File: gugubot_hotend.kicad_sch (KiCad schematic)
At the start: 79 parts, among them J1 Power +24V, J2 TEMP_SENSOR, J3 X_ENDSTOP, J4 PROBE, J5 FAN1, J6 FAN2, J7 Heater, J8 Extruder_motor, J9 USB_C_Receptacle_USB2.0, Q1 WST4041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

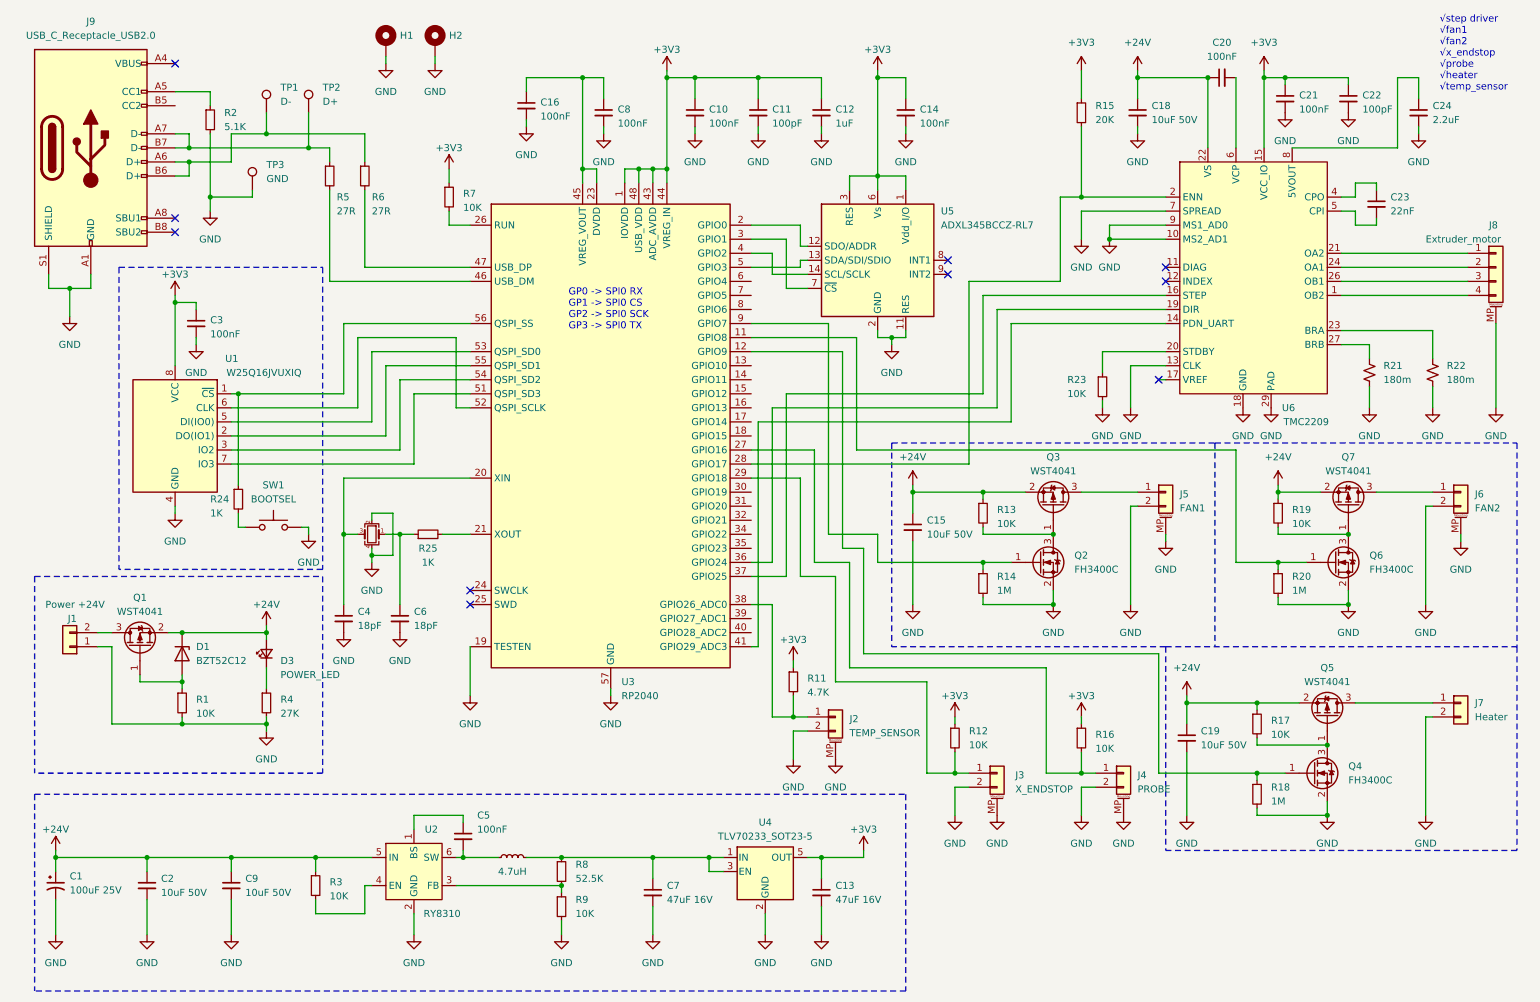
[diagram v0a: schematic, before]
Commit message: add hall board
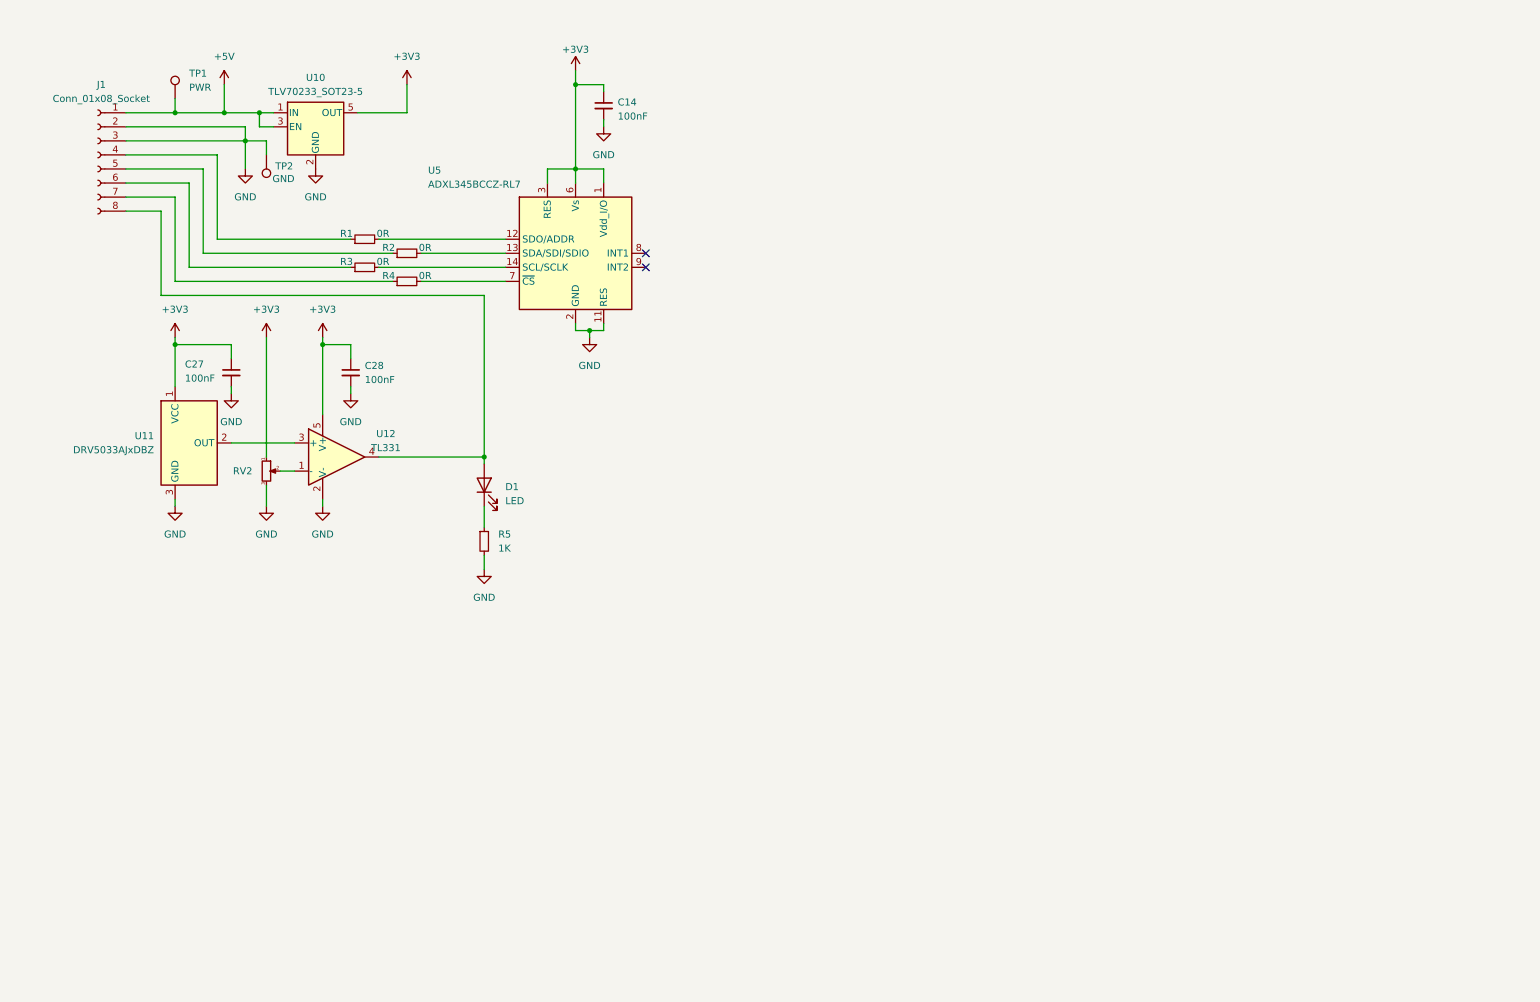
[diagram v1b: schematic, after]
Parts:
- removed C1: 100uF 25V, Capacitor_SMD:CP_Elec_6.3x5.8, symbol Device:C_Polarized_Small_US
- removed C10, C16, C20, C21, C3, C5, C8: 100nF, Capacitor_SMD:C_0402_1005Metric, symbol Device:C_Small
- removed C11, C22: 100pF, Capacitor_SMD:C_0402_1005Metric, symbol Device:C_Small
- removed C12: 1uF, Capacitor_SMD:C_0402_1005Metric, symbol Device:C_Small
- removed C13, C7: 47uF 16V, Capacitor_SMD:C_1210_3225Metric, symbol Device:C_Small
- removed C15, C18, C19, C2, C9: 10uF 50V, Capacitor_SMD:C_1210_3225Metric, symbol Device:C_Small
- removed C23: 22nF, Capacitor_SMD:C_0402_1005Metric, symbol Device:C_Small
- removed C24: 2.2uF, Capacitor_SMD:C_0402_1005Metric, symbol Device:C_Small
- removed C4, C6: 18pF, Capacitor_SMD:C_0402_1005Metric, symbol Device:C_Small
- removed D1: BZT52C12, Diode_SMD:D_SOD-123, symbol Diode:ZMMxx
- removed D3: POWER_LED, LED_SMD:LED_0603_1608Metric, symbol Device:LED_Small
- removed H1, H2: MountingHole_Pad, MountingHole:MountingHole_3.2mm_M3_Pad_Via, symbol Mechanical:MountingHole_Pad
- removed J1: Power +24V, TerminalBlock_TE-Connectivity:TerminalBlock_TE_282834-2_1x02_P2.54mm_Horizontal, symbol Connector_Generic:Conn_01x02
- removed J2: TEMP_SENSOR, Connector_GH:GH_1.25_1x02_Horizontal, symbol Connector_Generic_MountingPin:Conn_01x02_MountingPin
- removed J3: X_ENDSTOP, Connector_GH:GH_1.25_1x02_Horizontal, symbol Connector_Generic_MountingPin:Conn_01x02_MountingPin
- removed J4: PROBE, Connector_GH:GH_1.25_1x02_Horizontal, symbol Connector_Generic_MountingPin:Conn_01x02_MountingPin
- removed J5: FAN1, Connector_GH:GH_1.25_1x02_Horizontal, symbol Connector_Generic_MountingPin:Conn_01x02_MountingPin
- removed J6: FAN2, Connector_GH:GH_1.25_1x02_Horizontal, symbol Connector_Generic_MountingPin:Conn_01x02_MountingPin
- removed J7: Heater, TerminalBlock_TE-Connectivity:TerminalBlock_TE_282834-2_1x02_P2.54mm_Horizontal, symbol Connector_Generic:Conn_01x02
- removed J8: Extruder_motor, Connector_GH:GH_1.25_1x04_Veritical, symbol Connector_Generic_MountingPin:Conn_01x04_MountingPin
- removed J9: USB_C_Receptacle_USB2.0, Connector_USB:USB_C_Receptacle_G-Switch_GT-USB-7010ASV, symbol Connector:USB_C_Receptacle_USB2.0
- removed L1: 4.7uH, Inductor_SMD:L_1008_2520Metric, symbol Device:L_Small
- removed Q1, Q3, Q5, Q7: WST4041, Package_TO_SOT_SMD:SOT-23, symbol Device:Q_PMOS_GSD
- removed Q2, Q4, Q6: FH3400C, Package_TO_SOT_SMD:SOT-23, symbol Device:Q_NMOS_GSD
- removed R11: 4.7K, Resistor_SMD:R_0402_1005Metric, symbol Device:R_Small
- removed R12, R13, R16, R17, R19, R23, R7, R9: 10K, Resistor_SMD:R_0402_1005Metric, symbol Device:R_Small
- removed R14, R18, R20: 1M, Resistor_SMD:R_0402_1005Metric, symbol Device:R_Small
- removed R15: 20K, Resistor_SMD:R_0402_1005Metric, symbol Device:R_Small
- removed R21, R22: 180m, Resistor_SMD:R_1206_3216Metric, symbol Device:R_Small_US
- removed R24, R25: 1K, Resistor_SMD:R_0402_1005Metric, symbol Device:R_Small
- removed R6: 27R, Resistor_SMD:R_0402_1005Metric, symbol Device:R_Small
- removed R8: 52.5K, Resistor_SMD:R_0402_1005Metric, symbol Device:R_Small
- removed SW1: BOOTSEL, Button_Switch_SMD:SW_SPST_CK_RS282G05A3, symbol Switch:SW_Push
- removed TP3: GND, TestPoint:TestPoint_Pad_1.5x1.5mm, symbol Connector:TestPoint
- removed U1: W25Q16JVUXIQ, Package_SON:USON-8_3.0x2.0mm_P0.5mm, symbol Memory_Flash:W25Q32JVSS
- removed U2: RY8310, Package_TO_SOT_SMD:SOT-23-6, symbol Regulator_Switching:RY8310
- removed U3: RP2040, Package_DFN_QFN:QFN-56-1EP_7x7mm_P0.4mm_EP3.2x3.2mm, symbol MCU_RaspberryPi:RP2040
- removed U4: TLV70233_SOT23-5, Package_TO_SOT_SMD:SOT-23-5, symbol Regulator_Linear:TLV70233_SOT23-5
- removed U6: TMC2209, Package_DFN_QFN:QFN-28-1EP_5x5mm_P0.5mm_EP3.75x3.75mm, symbol Driver_Motor:TMC2209
- removed Y1: 12MHz, Oscillator:Oscillator_SMD_Kyocera_KC2520Z-4Pin_2.5x2.0mm, symbol Device:Crystal_GND24_Small
- added C27, C28: 100nF, Capacitor_SMD:C_0402_1005Metric, symbol Device:C_Small
- added D1: LED, LED_SMD:LED_0603_1608Metric, symbol Device:LED
- added J1: Conn_01x08_Socket, Connector_JST:JST_GH_SM08B-GHS-TB_1x08-1MP_P1.25mm_Horizontal, symbol Connector:Conn_01x08_Socket
- added RV2: R_Potentiometer_Small, Potentiometer_SMD:Potentiometer_Bourns_TC33X_Vertical, symbol Device:R_Potentiometer_Small
- added U10: TLV70233_SOT23-5, Package_TO_SOT_SMD:SOT-23-5, symbol Regulator_Linear:TLV70233_SOT23-5
- added U11: DRV5033AJxDBZ, Package_TO_SOT_SMD:SOT-23, symbol Sensor_Magnetic:DRV5033AJxDBZ
- added U12: TL331, Package_TO_SOT_SMD:SOT-23-5, symbol Comparator:TL331
- R1, R3: value 10K -> 0R
- R2: value 5.1K -> 0R
- R4: value 27K -> 0R
- R5: value 27R -> 1K
- TP1: value D- -> PWR; footprint TestPoint:TestPoint_Pad_1.5x1.5mm -> TestPoint:TestPoint_Pad_2.0x2.0mm
- TP2: value D+ -> GND; footprint TestPoint:TestPoint_Pad_1.5x1.5mm -> TestPoint:TestPoint_Pad_2.0x2.0mm
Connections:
- net +3V3: now also C27.1, C28.1, RV2.1, U10.5 (OUT), U11.1 (VCC), U12.5 (V+)
- net GND: now also R5.2, TP2.1, C27.2, C28.2, J1.2 (Pin_2), J1.3 (Pin_3), RV2.3, U10.2 (GND), U11.3 (GND), U12.2 (V-); no longer R1.2, R2.2, R4.2
- net at R1.1: now also J1.4 (Pin_4)
- net at R4.1: now also J1.7 (Pin_7)
- net +5V: now reaches TP1.1
- net +5V: now also J1.1 (Pin_1), U10.1 (IN), U10.3 (EN)
- net at R2.1: now also J1.5 (Pin_5)
- net at R5.1: now also D1.1 (K); no longer TP2.1
- net at U5.12 (SDO/ADDR): now also R1.2
- net at U5.7 (~{CS}): now also R4.2
- net at U5.14 (SCL/SCLK): now also R3.2
- net at U5.13 (SDA/SDI/SDIO): now also R2.2
- net +24V: no longer names the net of R3.1
- net +24V: now also J1.6 (Pin_6)
- new net: D1.2 (A), J1.8 (Pin_8), U12.4
- new net: RV2.2, U12.1 (-)
- new net: U11.2 (OUT), U12.3 (+)
- no-connect marks 10 -> 2
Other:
- note removed: "GP0 -> SPI0 RX GP1 -> SPI0 CS GP2 -> SPI0 SCK GP3 -> SPI0 TX"
- note removed: "√step driver √fan1 √fan2 √x_endstop √probe √heater √temp_sensor"
- moved on the sheet: C14, U5
